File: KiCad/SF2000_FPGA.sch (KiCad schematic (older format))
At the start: 10 parts, among them J3 Conn_02x03_Odd_Even, J4 Conn_02x01, J8 Conn_02x01, J9 Conn_02x01, U7 10M04SCE144

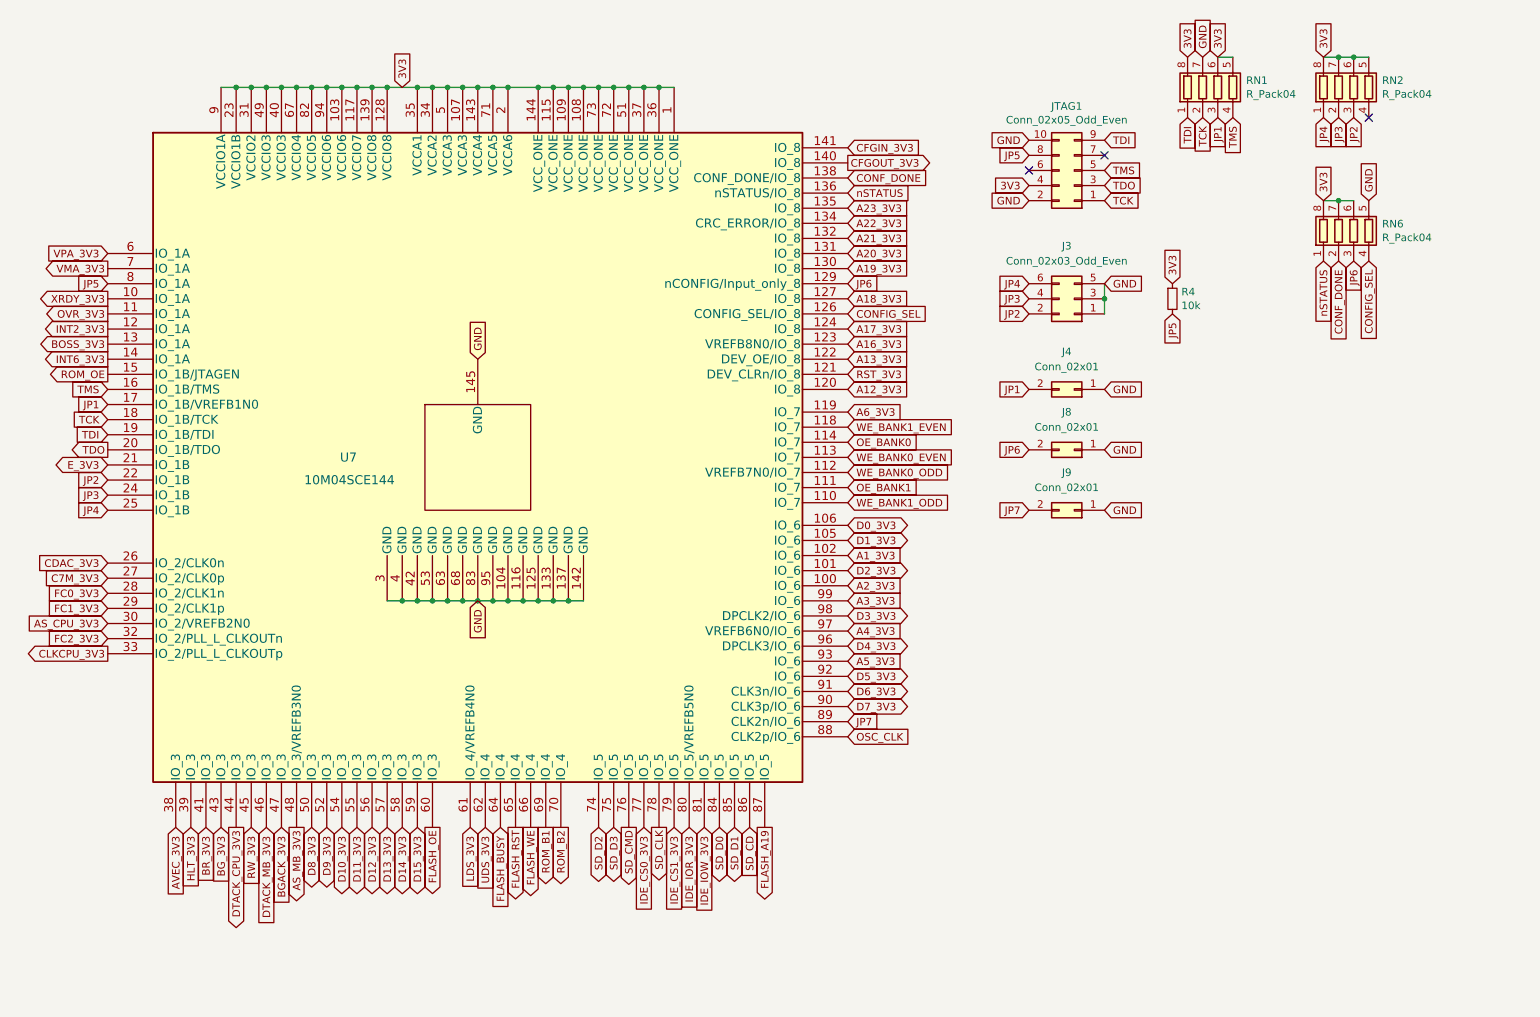
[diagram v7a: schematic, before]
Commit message: Fixed Switch and Jumper enumeration and silkscreen
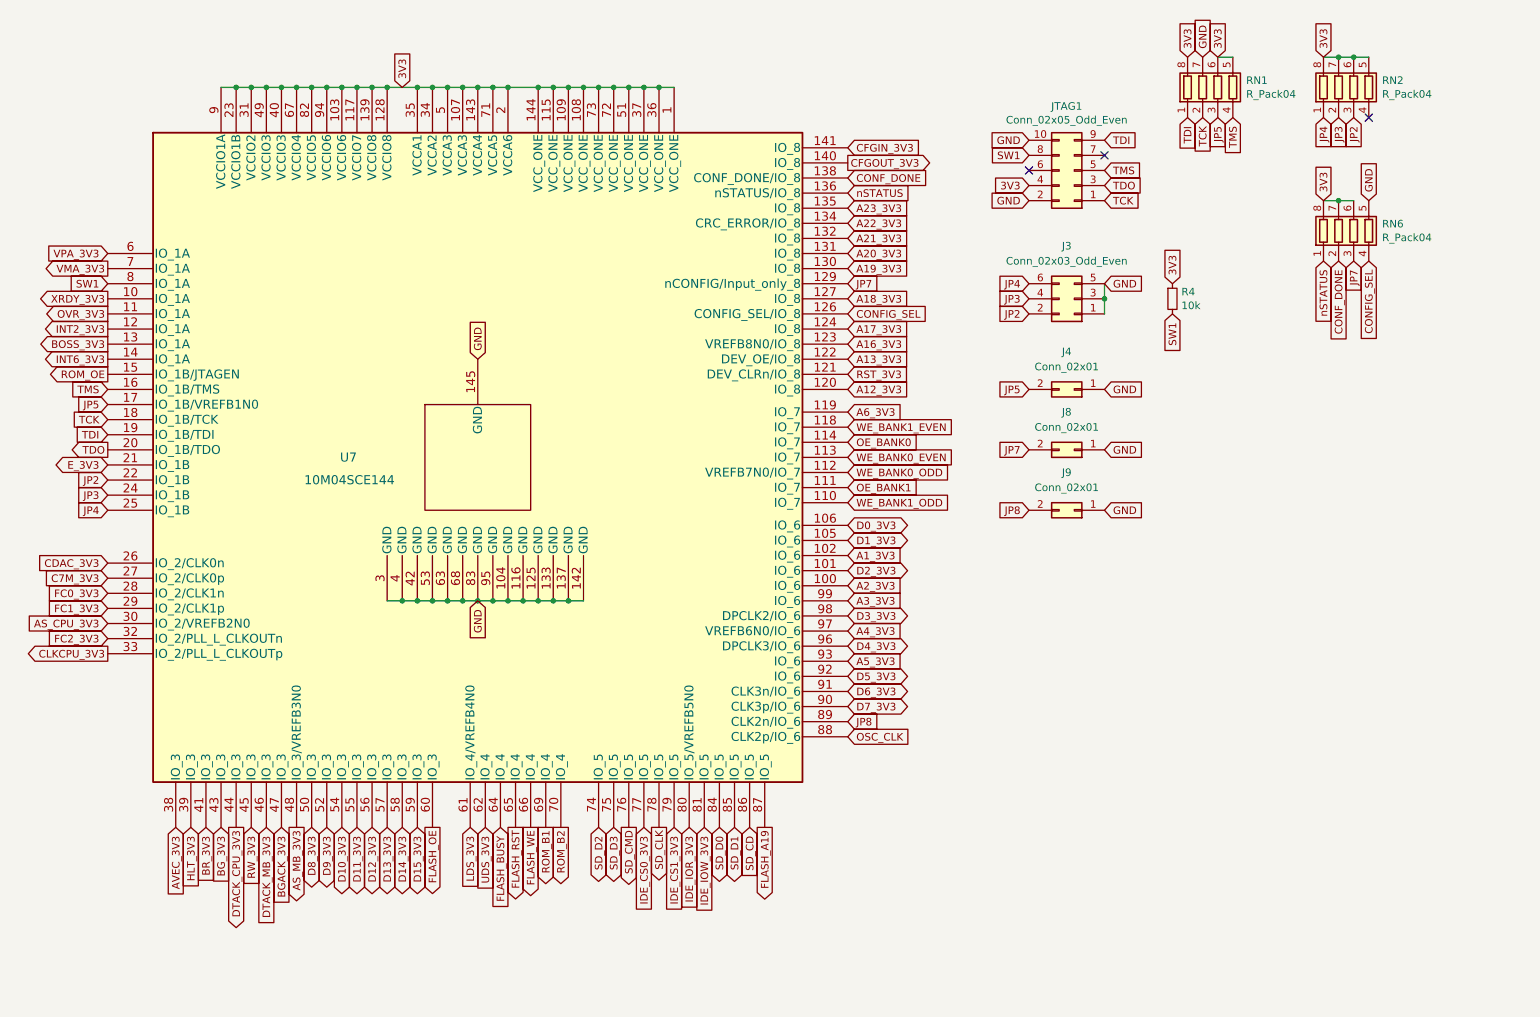
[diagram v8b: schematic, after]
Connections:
- net JP1 is gone; now on net JP5: J4.2 (Pin_2), RN1.3 (R3.1), U7.17 (IO_1B/VREFB1N0)
- net JP6 is gone; now on net JP7: J8.2 (Pin_2), RN6.3 (R3.1), U7.129 (nCONFIG/Input_only_8)
- net JP5: no longer JTAG1.8 (Pin_8), R4.2, U7.8 (IO_1A)
- net JP7: no longer J9.2 (Pin_2), U7.89 (CLK2n/IO_6)
- new net JP8: J9.2 (Pin_2), U7.89 (CLK2n/IO_6)
- new net SW1: JTAG1.8 (Pin_8), R4.2, U7.8 (IO_1A)
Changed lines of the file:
@@
 CONFIG_SEL
 Text GLabel 1350 2400 0    50   Input ~ 0
-JP5
-Text GLabel 7450 1550 0    50   Input ~ 0
+SW1
+Text GLabel 7450 3100 0    50   Input ~ 0
 JP5
 $Comp
@@
 Text GLabel 8800 1300 3    50   Input ~ 0
 TMS
+Text GLabel 8400 2600 3    50   Input ~ 0
+SW1
 Text GLabel 8700 1300 3    50   Input ~ 0
-JP1
-Text GLabel 8400 2600 3    50   Input ~ 0
 JP5
 Text GLabel 8600 900  1    50   Input ~ 0
@@
 Text GLabel 7950 3100 2    50   Input ~ 0
 GND
-Text GLabel 7450 3100 0    50   Input ~ 0
-JP1
+Text GLabel 7450 1550 0    50   Input ~ 0
+SW1
 Text GLabel 1350 3200 0    50   Input ~ 0
-JP1
+JP5
 Text GLabel 9600 1300 3    50   Input ~ 0
 JP2
@@
 GND
 Text GLabel 6250 2400 2    50   Input ~ 0
-JP6
+JP7
 $Comp
 L Connector_Generic:Conn_02x01 J8
@@
 GND
 Text GLabel 7450 3500 0    50   Input ~ 0
-JP6
+JP7
 $Comp
 L Connector_Generic:Conn_02x01 J9
@@
 GND
 Text GLabel 7450 3900 0    50   Input ~ 0
-JP7
+JP8
 Text GLabel 6250 5300 2    50   Input ~ 0
-JP7
+JP8
 Text GLabel 3500 6000 3    50   Output ~ 0
 FLASH_OE
@@
 Connection ~ 9500 1850
 Text GLabel 9600 2250 3    50   Input ~ 0
-JP6
+JP7
 $EndSCHEMATC
